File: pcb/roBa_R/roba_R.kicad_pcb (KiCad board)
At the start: 2 copper layers, 123.9 x 94.5 mm, 50 parts, among them J2 Conn_01x01-Connector_Generic, J3 Conn_01x01-Connector_Generic, J4 Conn_01x01-Connector_Generic, J5 Conn_01x01-Connector_Generic, J6 Conn_01x01-Connector_Generic, J7 Conn_01x01-Connector_Generic, SW1 SW_PUSH, SW10 SW_PUSH, SW11 SW_PUSH, SW12 SW_PUSH, SW13 SW_PUSH, SW14 SW_PUSH, SW15 SW_PUSH, SW16 SW_PUSH, SW17 SW_PUSH, SW18 SW_PUSH, SW19 SW_PUSH, SW2 SW_PUSH, SW20 SW_PUSH, SW21 SW_SPDT, SW3 SW_PUSH, SW4 SW_PUSH, SW5 SW_PUSH, SW6 SW_PUSH, SW7 SW_PUSH, SW8 SW_PUSH, SW9 SW_PUSH

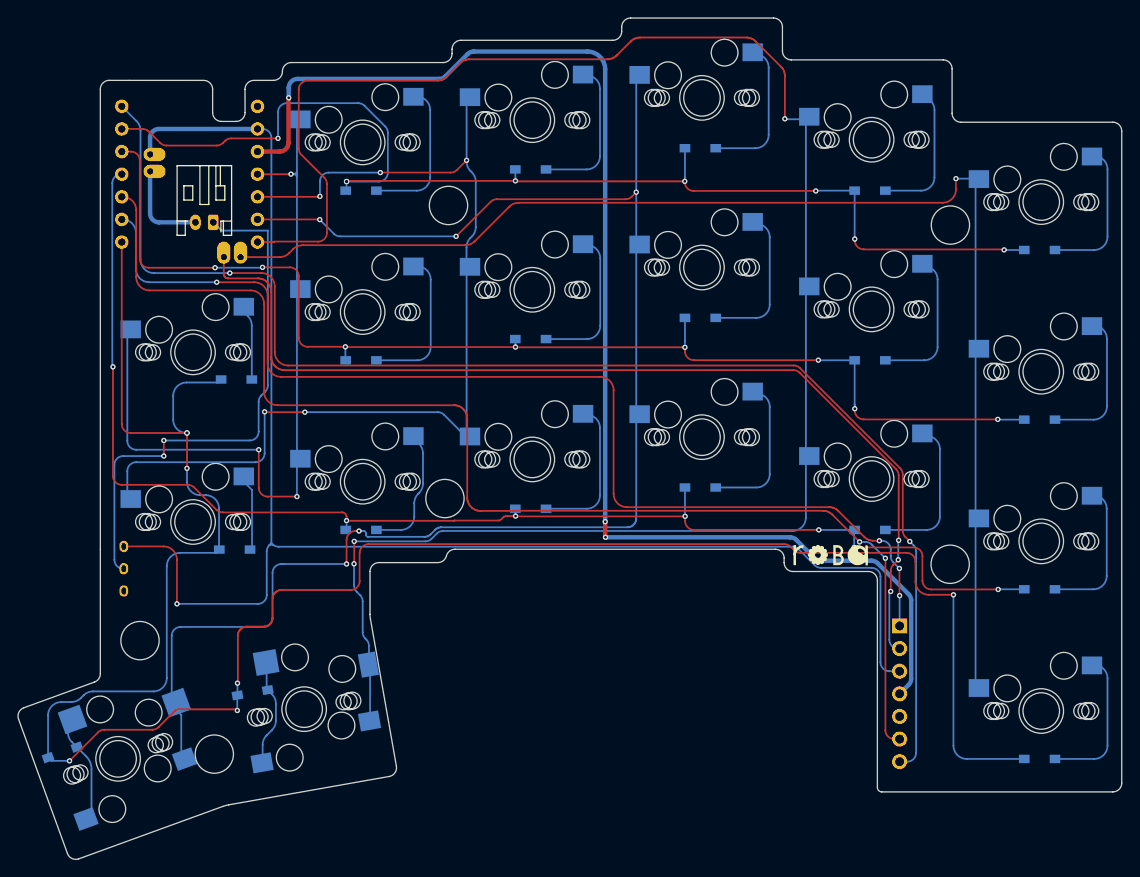
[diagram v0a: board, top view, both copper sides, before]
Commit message: fixed hole size for springpin
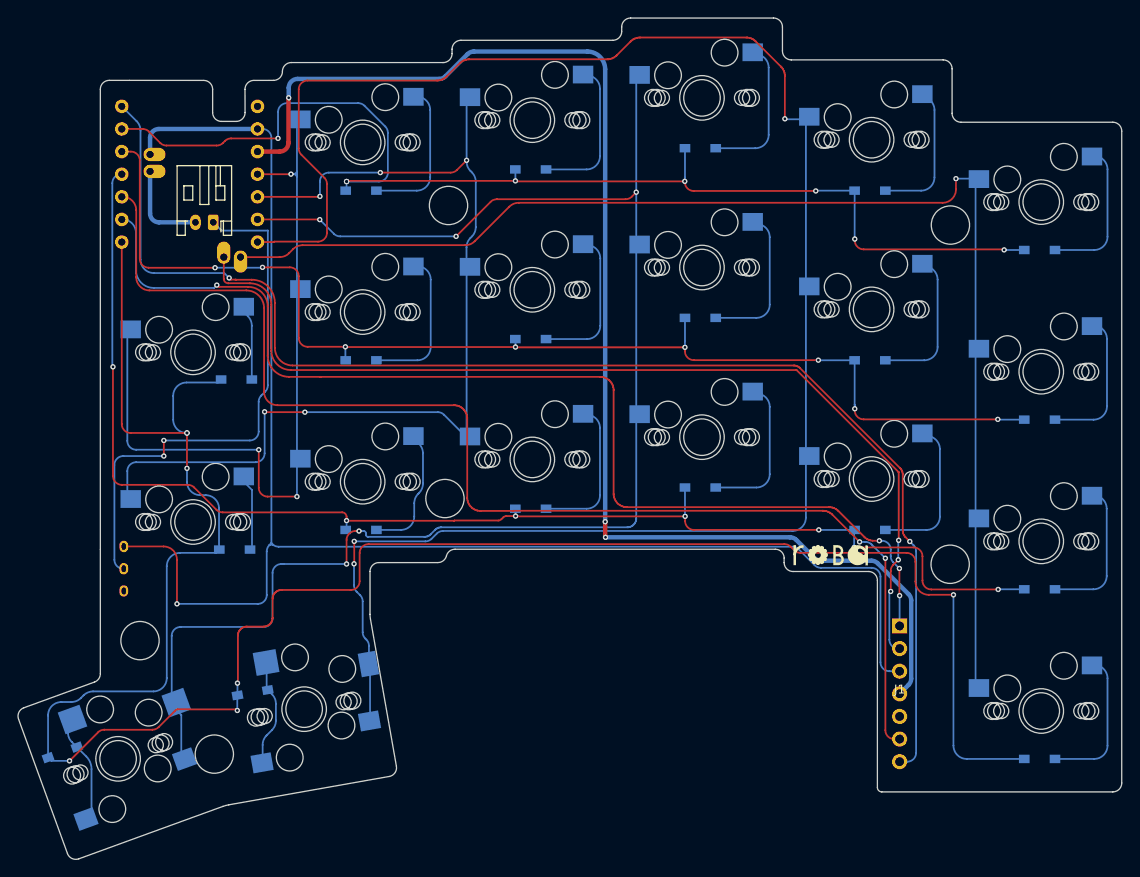
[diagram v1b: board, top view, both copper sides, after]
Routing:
- net MOTION: track 152.8 -> 151.6 mm
- net CS: track 112.7 -> 111.9 mm
- net SCLK: track 125.3 -> 124.8 mm

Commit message: fixed
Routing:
- net Row1: track 134.4 -> 134.9 mm
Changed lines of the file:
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@@
 		(fp_arc
 			(start 1.300995 -8.248791)
-			(mid 1.848289 -8.041024)
+			(mid 1.848288 -8.041026)
 			(end 2.162199 -7.546904)
 			(stroke
@@
 		)
 		(pad "20" thru_hole oval
-			(at -4.445 10.183)
+			(at -4.445 10.183 270)
 			(size 2.5 1.5)
 			(drill 0.8128
@@
 		)
 		(pad "21" thru_hole oval
-			(at -4.445 8.278)
+			(at -4.445 8.278 90)
 			(size 2.5 1.5)
 			(drill 0.8128
@@
 	)
 	(segment
-		(start 146.48 73.75)
-		(end 127.59 73.75)
+		(start 105.030001 67.920001)
+		(end 102.279007 67.920001)
 		(width 0.2)
 		(layer "F.Cu")
@@
 	)
 	(segment
-		(start 119.825 68.975)
-		(end 119.817999 68.982001)
+		(start 113.855106 69.274894)
+		(end 113.642893 69.487107)
 		(width 0.2)
 		(layer "F.Cu")
@@
 	)
 	(segment
-		(start 185.59 81.44)
-		(end 201.3 81.44)
+		(start 146.48 73.75)
+		(end 127.59 73.75)
 		(width 0.2)
 		(layer "F.Cu")
@@
 	)
 	(segment
-		(start 113.855106 69.274894)
-		(end 113.642893 69.487107)
+		(start 185.59 81.44)
+		(end 201.3 81.44)
 		(width 0.2)
 		(layer "F.Cu")
@@
 	)
 	(segment
-		(start 106.597107 69.487107)
-		(end 105.322894 68.212894)
+		(start 180.21 74.88)
+		(end 166.5 74.88)
 		(width 0.2)
 		(layer "F.Cu")
@@
 	)
 	(segment
-		(start 119.817999 68.982001)
-		(end 114.562213 68.982001)
+		(start 201.3 81.44)
+		(end 201.36 81.5)
 		(width 0.2)
 		(layer "F.Cu")
@@
 	)
 	(segment
-		(start 180.21 74.88)
-		(end 166.5 74.88)
+		(start 107.011321 69.487107)
+		(end 105.737108 68.212894)
 		(width 0.2)
 		(layer "F.Cu")
@@
 	)
 	(segment
-		(start 201.3 81.44)
-		(end 201.36 81.5)
+		(start 112.935786 69.78)
+		(end 107.718428 69.78)
 		(width 0.2)
 		(layer "F.Cu")
@@
 	)
 	(segment
-		(start 104.615787 67.920001)
-		(end 102.279007 67.920001)
+		(start 119.817999 68.982001)
+		(end 114.562213 68.982001)
 		(width 0.2)
 		(layer "F.Cu")
@@
 	)
 	(segment
-		(start 112.935786 69.78)
-		(end 107.304214 69.78)
+		(start 119.825 68.975)
+		(end 119.817999 68.982001)
 		(width 0.2)
 		(layer "F.Cu")
@@
 	)
 	(arc
-		(start 113.642893 69.487107)
-		(mid 113.318469 69.70388)
-		(end 112.935786 69.78)
+		(start 105.030001 67.920001)
+		(mid 105.412684 67.996121)
+		(end 105.737108 68.212894)
 		(width 0.2)
 		(layer "F.Cu")
@@
 	)
 	(arc
-		(start 114.562213 68.982001)
-		(mid 114.17953 69.058121)
-		(end 113.855106 69.274894)
+		(start 113.642893 69.487107)
+		(mid 113.318469 69.70388)
+		(end 112.935786 69.78)
 		(width 0.2)
 		(layer "F.Cu")
@@
 	)
 	(arc
-		(start 107.304214 69.78)
-		(mid 106.92153 69.70388)
-		(end 106.597107 69.487107)
+		(start 114.562213 68.982001)
+		(mid 114.17953 69.058121)
+		(end 113.855106 69.274894)
 		(width 0.2)
 		(layer "F.Cu")
@@
 	)
 	(arc
-		(start 105.322894 68.212894)
-		(mid 104.99847 67.996121)
-		(end 104.615787 67.920001)
+		(start 107.718428 69.78)
+		(mid 107.335745 69.70388)
+		(end 107.011321 69.487107)
 		(width 0.2)
 		(layer "F.Cu")
@@
 	)
 	(segment
+		(start 116.763785 84.362001)
+		(end 115.309151 84.362001)
+		(width 0.2)
+		(layer "B.Cu")
+		(net 5)
+	)
+	(segment
 		(start 184.5725 93.895001)
 		(end 180.515001 93.895001)
@@
 	)
 	(segment
+		(start 114.602044 84.069108)
+		(end 114.325829 83.792893)
+		(width 0.2)
+		(layer "B.Cu")
+		(net 5)
+	)
+	(segment
 		(start 184.59 99.34)
 		(end 184.59 98.92)
@@
 	)
 	(segment
-		(start 118.04 83.5)
-		(end 118.08 83.46)
-		(width 0.2)
-		(layer "B.Cu")
-		(net 5)
-	)
-	(segment
-		(start 112.75 83.5)
-		(end 118.04 83.5)
+		(start 200.682501 100.562501)
+		(end 200.65 100.53)
 		(width 0.2)
 		(layer "B.Cu")
@@
 	)
 	(segment
-		(start 200.682501 100.562501)
-		(end 200.65 100.53)
+		(start 127.39 93.862501)
+		(end 127.4225 93.895001)
 		(width 0.2)
 		(layer "B.Cu")
@@
 	)
 	(segment
-		(start 127.39 93.862501)
-		(end 127.4225 93.895001)
+		(start 118.08 83.46)
+		(end 117.470892 84.069108)
 		(width 0.2)
 		(layer "B.Cu")
@@
 	)
 	(segment
+		(start 113.618722 83.5)
+		(end 112.75 83.5)
+		(width 0.2)
+		(layer "B.Cu")
+		(net 5)
+	)
+	(arc
+		(start 114.602044 84.069108)
+		(mid 114.926467 84.285881)
+		(end 115.309151 84.362001)
+		(width 0.2)
+		(layer "B.Cu")
+		(net 5)
+	)
+	(arc
+		(start 114.325829 83.792893)
+		(mid 114.001406 83.57612)
+		(end 113.618722 83.5)
+		(width 0.2)
+		(layer "B.Cu")
+		(net 5)
+	)
+	(arc
+		(start 116.763785 84.362001)
+		(mid 117.146468 84.285881)
+		(end 117.470892 84.069108)
+		(width 0.2)
+		(layer "B.Cu")
+		(net 5)
+	)
+	(segment
 		(start 133.62 112.945001)
 		(end 130.8725 112.945001)
@@
 	)
 	(segment
-		(start 113.784407 84.1)
+		(start 113.370193 84.1)
 		(end 105.882951 84.1)
 		(width 0.2)
@@
 	(segment
 		(start 114.334407 84.65)
-		(end 113.784407 84.1)
+		(end 114.0773 84.392893)
 		(width 0.2)
 		(layer "B.Cu")
@@
 		(width 0.2)
 		(layer "B.Cu")
+		(net 27)
+	)
+	(arc
+		(start 114.0773 84.392893)
+		(mid 113.752877 84.17612)
+		(end 113.370193 84.1)
+		(width 0.2)
+		(layer "B.Cu")

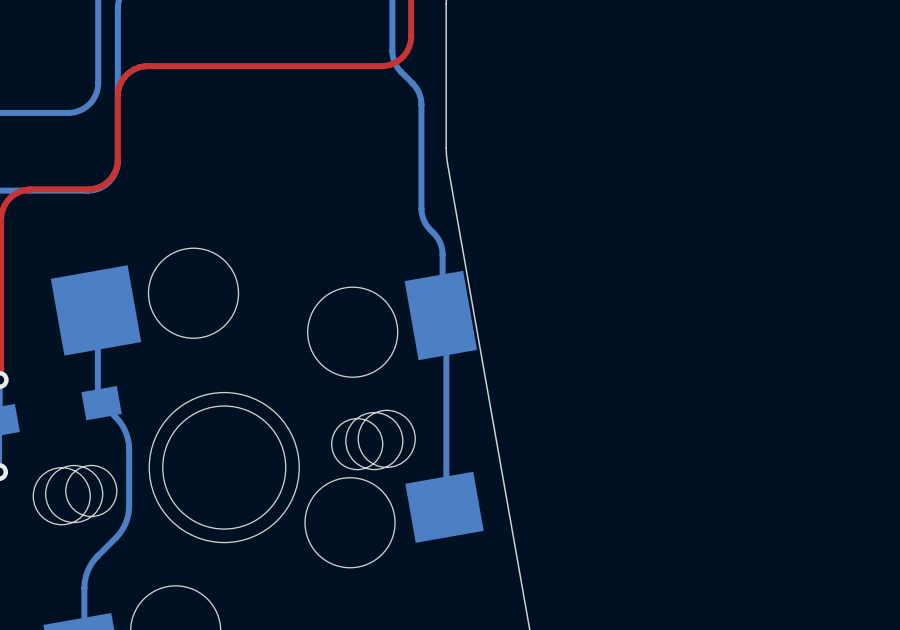
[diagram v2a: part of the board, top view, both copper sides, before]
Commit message: add fp and symbol
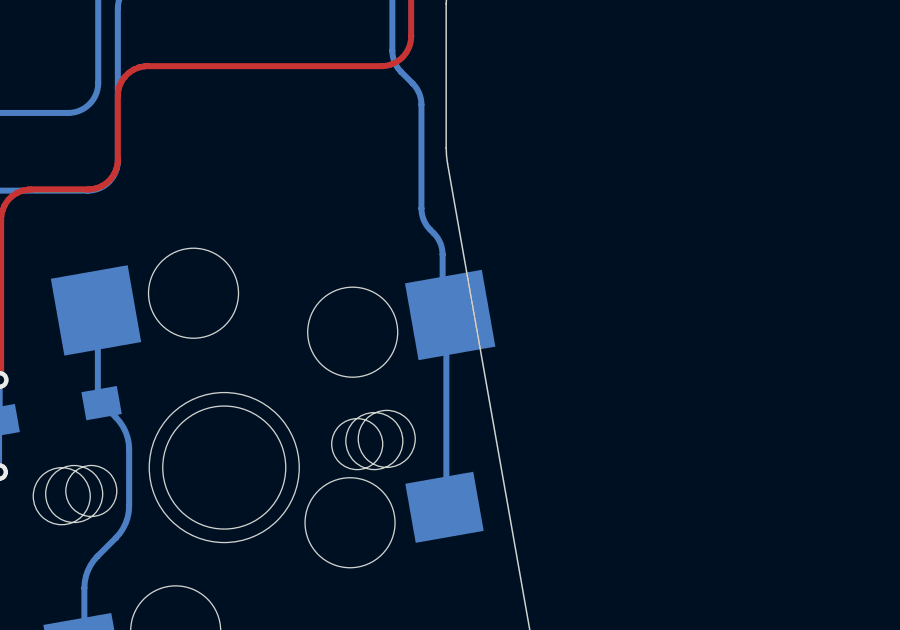
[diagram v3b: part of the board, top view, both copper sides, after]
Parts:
- BT1: footprint note96e:JST_PH_S2B-PH-K_custom -> roBa:JST_PH_S2B-PH-K_custom
- D1, D10, D11, D12, D13, D14, D15, D16, D17, D18, D19, D2, D20, D3, D4, D5, D6, D7, D8, D9: footprint note96e:Diode_SMD -> roBa:Diode_SMD
- J1: footprint myfootprintLibrary:pmw3610_connector -> roBa:pmw3610_connector
- SW1, SW10, SW11, SW13, SW14, SW15, SW17, SW18, SW19, SW2, SW20, SW3, SW4, SW5, SW6, SW7, SW8, SW9: footprint myfootprintLibrary:SW_MX -> roBa:SW_MX
- SW12, SW16: footprint myfootprintLibrary:SW_MX_Choc -> roBa:SW_MX_Choc
- SW21: footprint note96e:TGSW_MSK-12D19 -> roBa:TGSW_MSK-12D19
- U1: footprint myfootprintLibrary:XIAO_nRF52840_wBAT_wNFC -> roBa:XIAO_nRF52840_wBAT_wNFC
